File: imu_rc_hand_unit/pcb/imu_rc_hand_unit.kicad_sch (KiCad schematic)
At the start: 70 parts, among them J1 USB_C_Receptacle_USB2.0_16P, J2 JST SH1.0, Q1 AO3400A, Q2 AO3400A, Q3 AO3401A, Q4 AO3400A, Q5 AO3401A, Q6 BSS138, SW1 SW_SPDT, U2 MCP73831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

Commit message: add library kicad support
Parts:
- D7: footprint MyLibrary:LED_D5.0mm-4_RKGB -> IMURCLibrary:LED_D5.0mm-4_RKGB
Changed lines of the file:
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@@
 			)
 		)
-		(property "Footprint" "MyLibrary:LED_D5.0mm-4_RKGB"
+		(property "Footprint" "IMURCLibrary:LED_D5.0mm-4_RKGB"
 			(at 222.25 97.79 0)
 			(effects

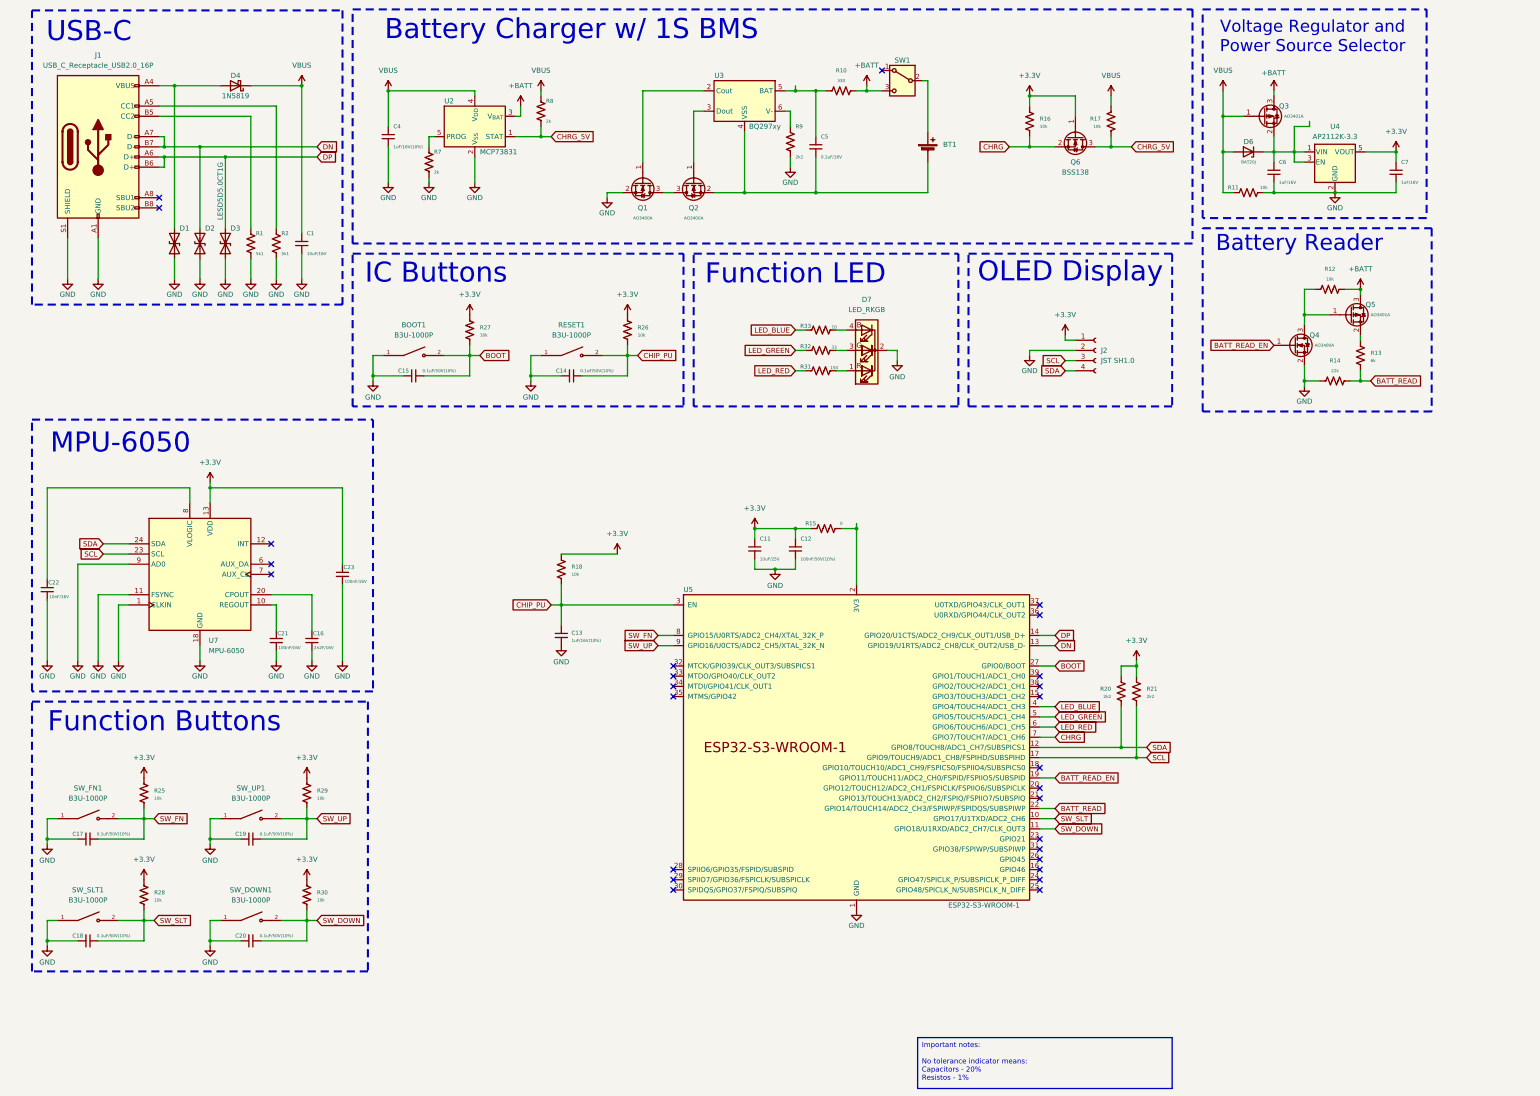
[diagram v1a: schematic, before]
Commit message: commit #10
created and added LSM6DSO to PCB
Changed MPU to LSM6
Added back UART converter
Added battery reader module
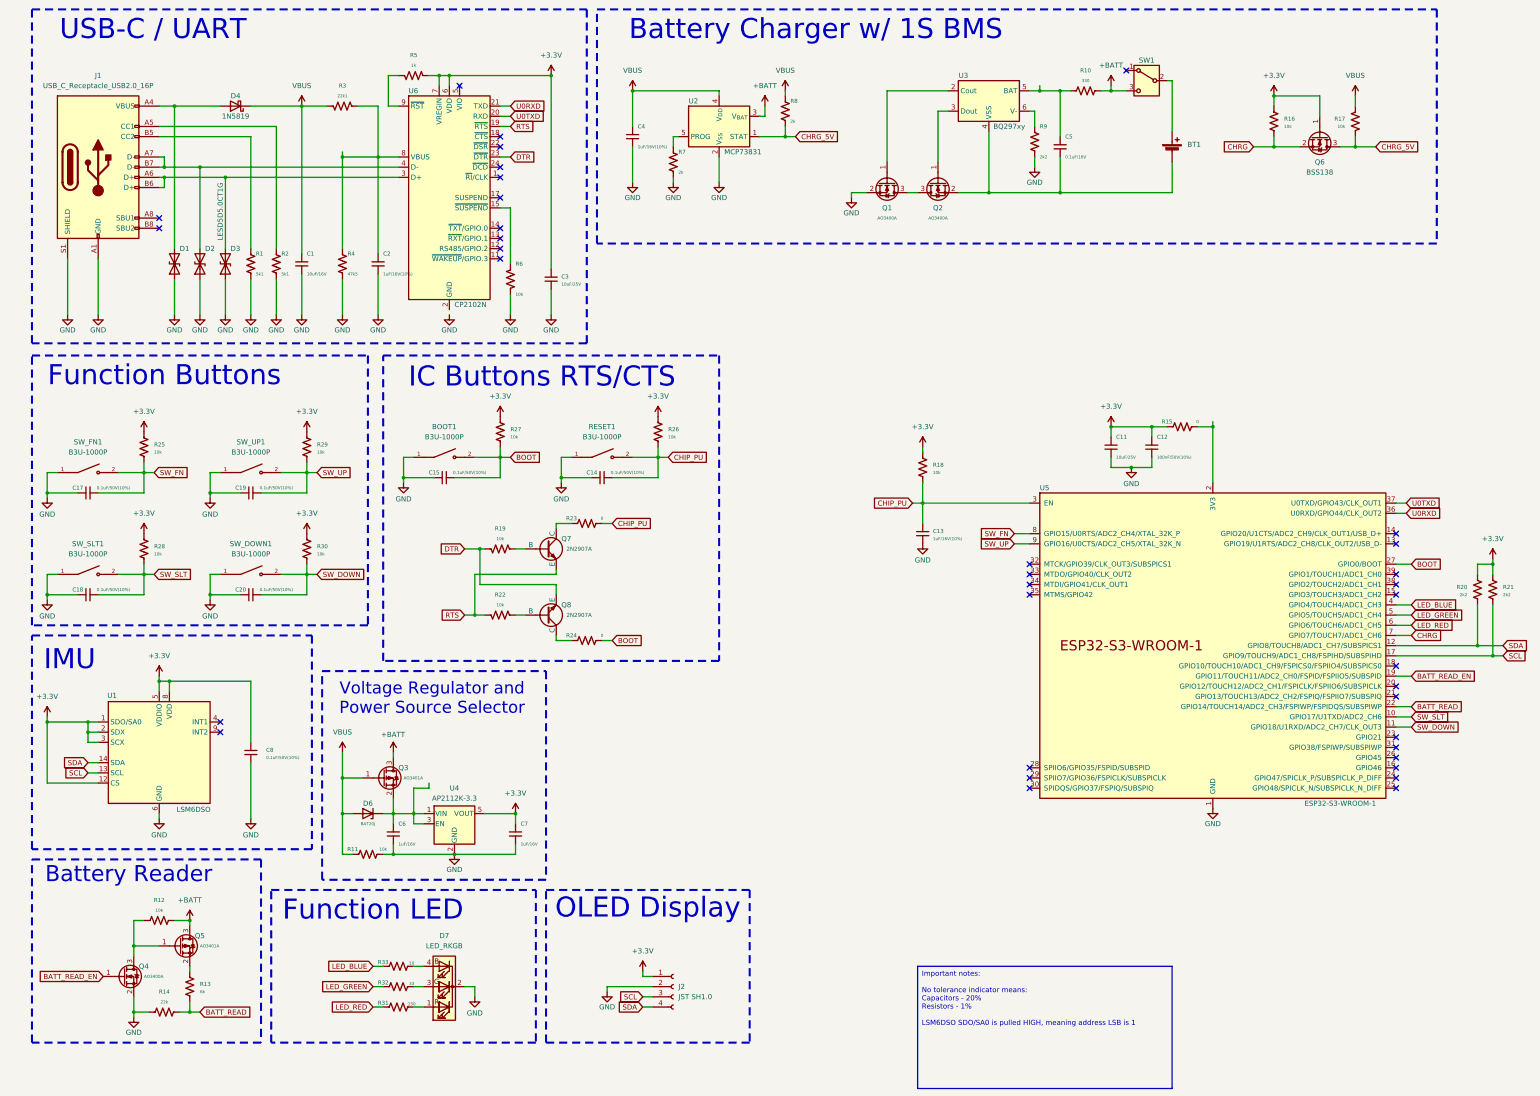
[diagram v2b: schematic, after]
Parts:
- removed C16: 2n2F/16V, Capacitor_SMD:C_0805_2012Metric, symbol Device:C_Small
- removed C21, C23: 100nF/16V, Capacitor_SMD:C_0805_2012Metric, symbol Device:C_Small
- removed C22: 10nF/16V, Capacitor_SMD:C_0805_2012Metric, symbol Device:C_Small
- removed U7: MPU-6050, Sensor_Motion:InvenSense_QFN-24_4x4mm_P0.5mm, symbol Sensor_Motion:MPU-6050
- added C2: 1uF/16V(10%), Capacitor_SMD:C_0603_1608Metric, symbol Device:C_Small
- added C3: 10uF/25V, Capacitor_SMD:C_0603_1608Metric, symbol Device:C_Small
- added C8: 0.1uF/50V(10%), Capacitor_SMD:C_0805_2012Metric, symbol Device:C_Small
- added Q7, Q8: 2N2907A, Package_TO_SOT_SMD:SOT-23, symbol Simulation_SPICE:NPN
- added R19, R22, R6: 10k, Resistor_SMD:R_0805_2012Metric, symbol Device:R_US
- added R23, R24: 0, Resistor_SMD:R_1206_3216Metric, symbol Device:R_US
- added R3: 22k1, Resistor_SMD:R_0805_2012Metric, symbol Device:R_US
- added R4: 47k5, Resistor_SMD:R_0805_2012Metric, symbol Device:R_US
- added R5: 1k, Resistor_SMD:R_0805_2012Metric, symbol Device:R_US
- added U1: LSM6DSO, IMURCLibrary:LGA-14L_3x2.5mm_P0.5mm, symbol Sensor_Motion:LSM6DS3
- added U6: CP2102N, Package_DFN_QFN:QFN-24-1EP_4x4mm_P0.5mm_EP2.6x2.6mm, symbol Interface_USB:CP2102N-Axx-xQFN24
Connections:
- net +3.3V: now also C3.2, C8.1, R5.2, U1.1 (SDO/SA0), U1.12 (CS), U1.2 (SDX), U1.3 (SCX), U1.5 (VDDIO), U1.8 (VDD), U6.6 (VDD), U6.7 (VREGIN)
- net BOOT: now also R24.2
- net CHIP_PU: now also R23.2
- net GND: now also C2.2, C3.1, C8.2, R4.1, R6.2, U1.6 (GND), U1.7 (GND)
- net SCL: now also U1.13 (SCL)
- net SDA: now also U1.14 (SDA)
- net VBUS: now also R3.2
- net U0RXD: now reaches U5.36 (U0RXD/GPIO44/CLK_OUT2)
- net U0RXD: now also U6.21 (TXD)
- net U0TXD: now reaches U5.37 (U0TXD/GPIO43/CLK_OUT1)
- net U0TXD: now also U6.20 (RXD)
- net DN: no longer names the net of D2.2 (A2), J1.A7 (D-), J1.B7 (D-)
- net DN: now also U6.4 (D-); no longer U5.13 (GPIO19/U1RTS/ADC2_CH8/CLK_OUT2/USB_D-)
- net DP: no longer names the net of D3.2 (A2), J1.A6 (D+), J1.B6 (D+)
- net DP: now also U6.3 (D+); no longer U5.14 (GPIO20/U1CTS/ADC2_CH9/CLK_OUT1/USB_D+)
- new net: C2.1, R3.1, R4.2, U6.8 (VBUS)
- new net: Q7.2 (B), R19.2
- new net: Q8.2 (B), R22.2
- new net: Q7.1 (C), R23.1
- new net: R6.1, U6.15 (~{SUSPEND})
- new net: U6.2 (GND), U6.25 (GND)
- new net: R5.1, U6.9 (~{RST})
- new net: Q8.1 (C), R24.1
- new net DTR: Q8.3 (E), R19.1, U6.23 (~{DTR})
- new net RTS: Q7.3 (E), R22.1, U6.19 (~{RTS})
- no-connect marks 27 -> 36
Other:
- note added: "IC Buttons RTS/CTS"
- note added: "IMU"
- note added: "USB-C / UART"
- note removed: "IC Buttons"
- note removed: "MPU-6050"
- note removed: "USB-C"
- moved on the sheet: BOOT1, BT1, C1, C11, C12, C13, C14, C15, C17, C18, C19, C20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

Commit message: commit #12
added cost prevision table #2
minor changes overall
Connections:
- net BATT_READ_EN: now also U5.23 (GPIO21); no longer U5.19 (GPIO11/TOUCH11/ADC2_CH0/FSPID/FSPIIO5/SUBSPID)
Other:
- moved on the sheet: R20, R21

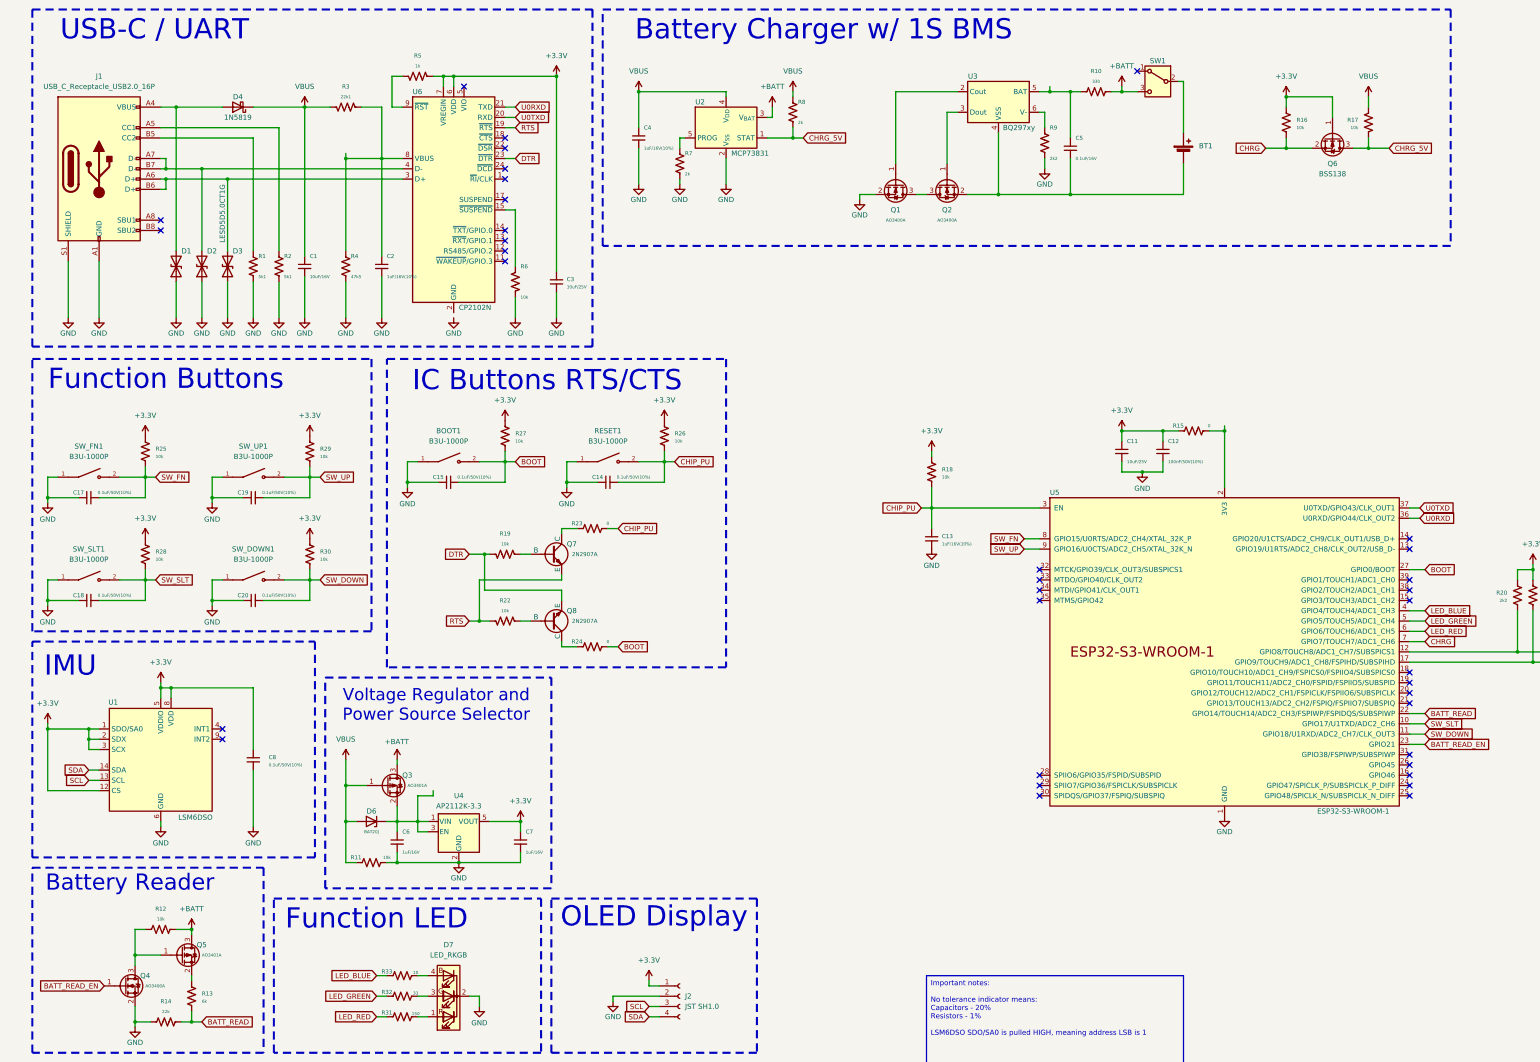
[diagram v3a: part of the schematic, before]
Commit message: commit #13
refactored component values to more popular values
refactored components for less obsolete/more popular choices

bug fix TG1WDT_SYS_RESET
bug fix move() func

implement additional screen features
better readability
refactored navigation
added sensitivity option
added led information
added car status
added data print
added reset option

refactored board costs table
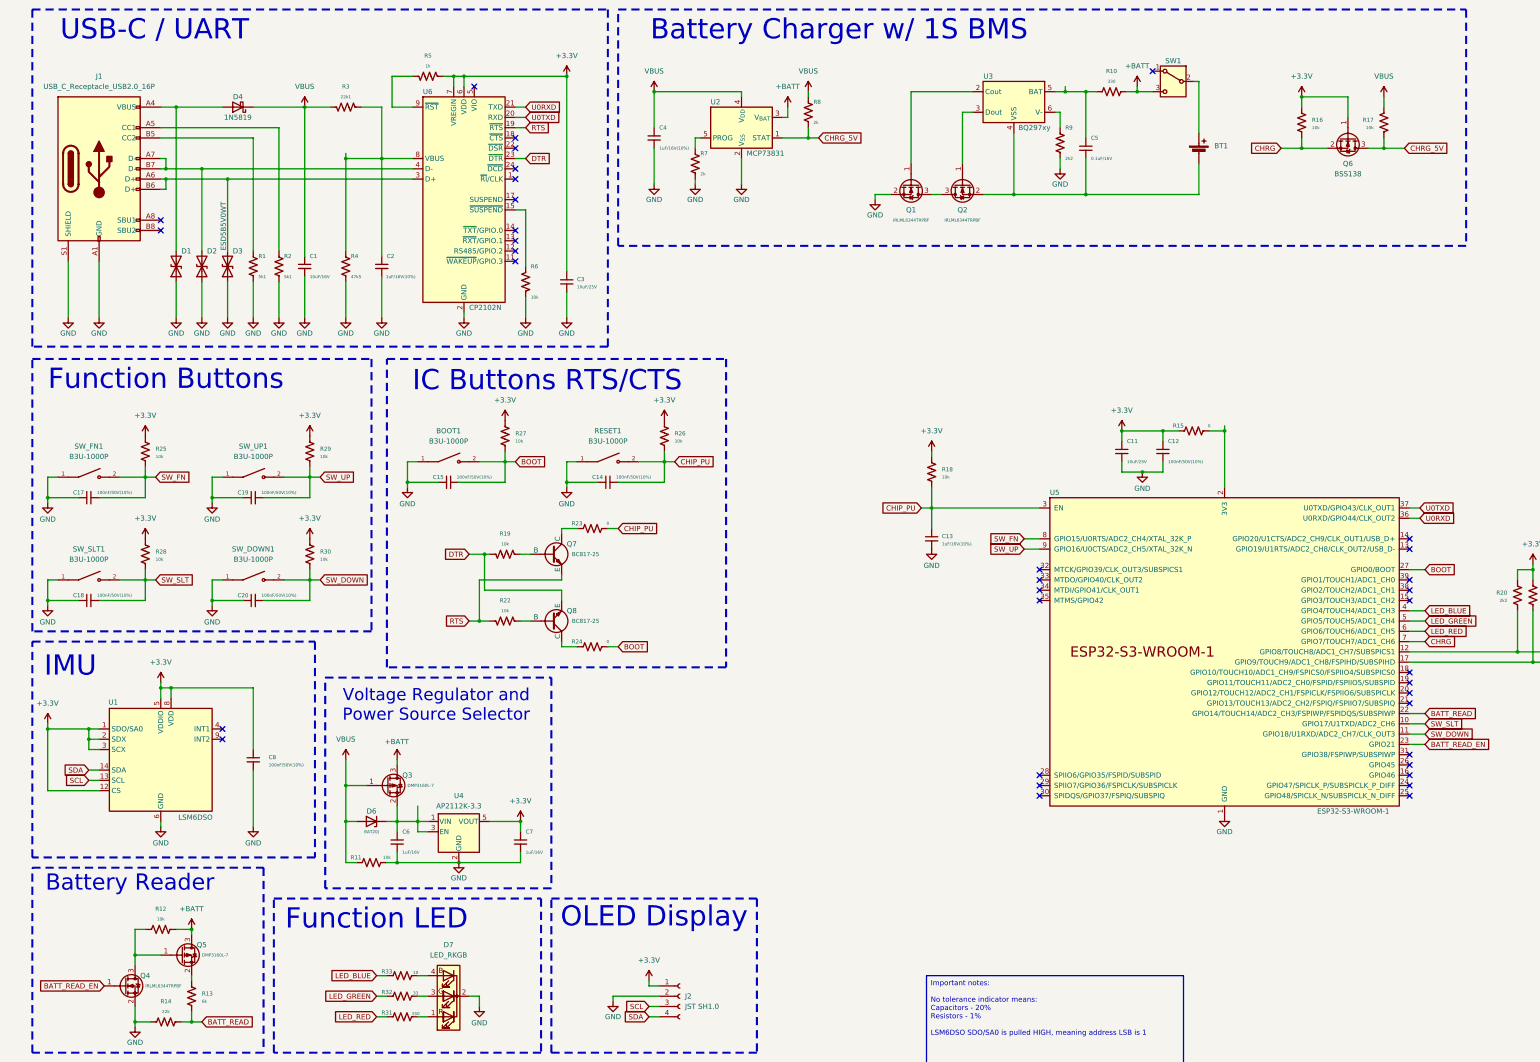
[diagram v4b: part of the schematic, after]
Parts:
- C14, C15, C17, C18, C19, C20, C8: value 0.1uF/50V(10%) -> 100nF/50V(10%)
- D3: value LESD5D5.0CT1G -> ESD5B5V0WT
- Q1, Q2, Q4: value AO3400A -> IRLML6344TRPBF
- Q3, Q5: value AO3401A -> DMP3160L-7
- Q7, Q8: value 2N2907A -> BC817-25
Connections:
- net GND: now also U6.2 (GND), U6.25 (GND)
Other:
- moved on the sheet: BT1, C3, C4, C5, Q1, Q2, Q6, R10, R16, R17, R5, R6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

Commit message: commit #27
revision for hand unit complete (board is ready)
board for proximity sensors in series
minor revision in encoder board
progressing work in car board
added essential libraries support for 3D components
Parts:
- J2: footprint Connector_JST:JST_SH_SM04B-SRSS-TB_1x04-1MP_P1.00mm_Horizontal -> IMURCLibrary:JST_SH_SM04B-SRSS-TB_1x04-1MP_P1.00mm_Horizontal
